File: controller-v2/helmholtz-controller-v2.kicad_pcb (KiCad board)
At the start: 2 copper layers, 72.7 x 72.1 mm, 60 parts, among them J1 Screw_Terminal_01x02, J2 Screw_Terminal_01x02, J3 Screw_Terminal_01x02, J4 Screw_Terminal_01x02, J5 Conn_01x04, U1 BDS63150AFM, U2 BDS63150AFM, U3 INA226, U4 INA226, U5 BDS63150AFM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

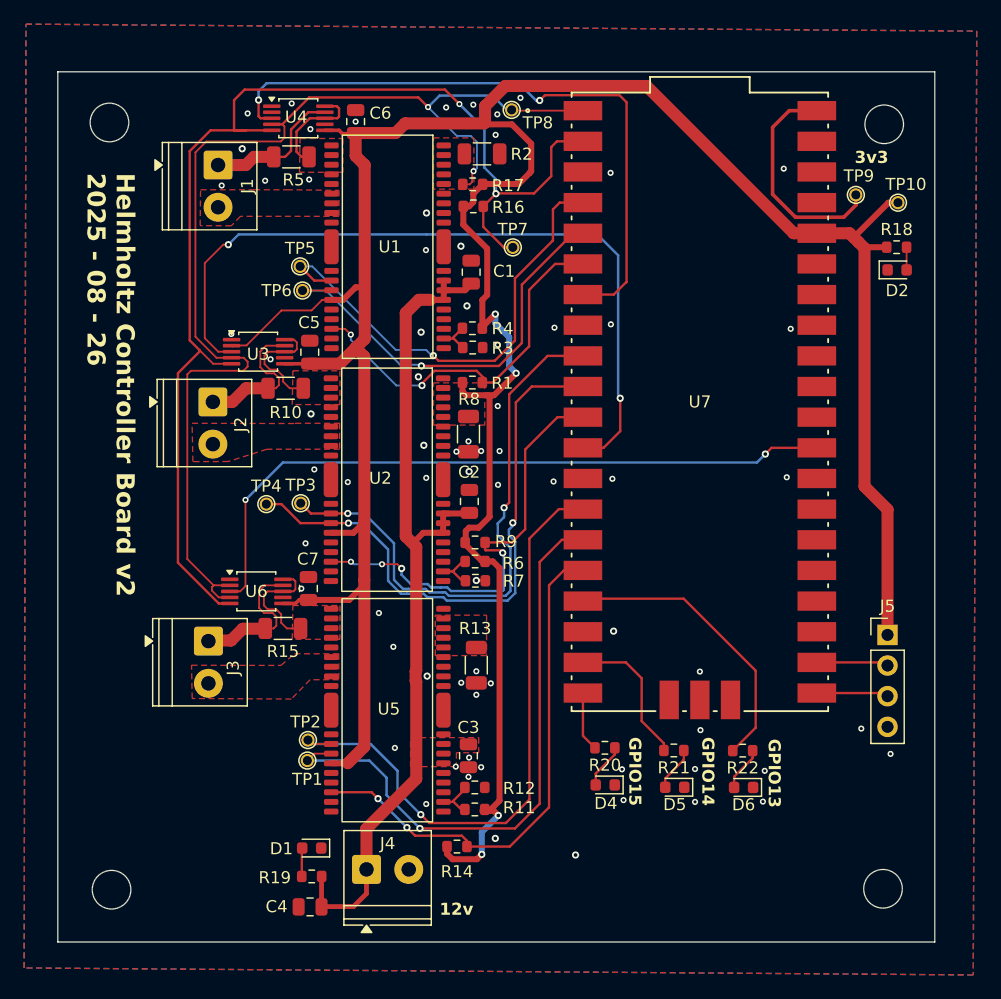
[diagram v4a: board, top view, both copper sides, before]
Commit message: Final cleanup of board before fab.
Did some polishing on layout for better power flow.
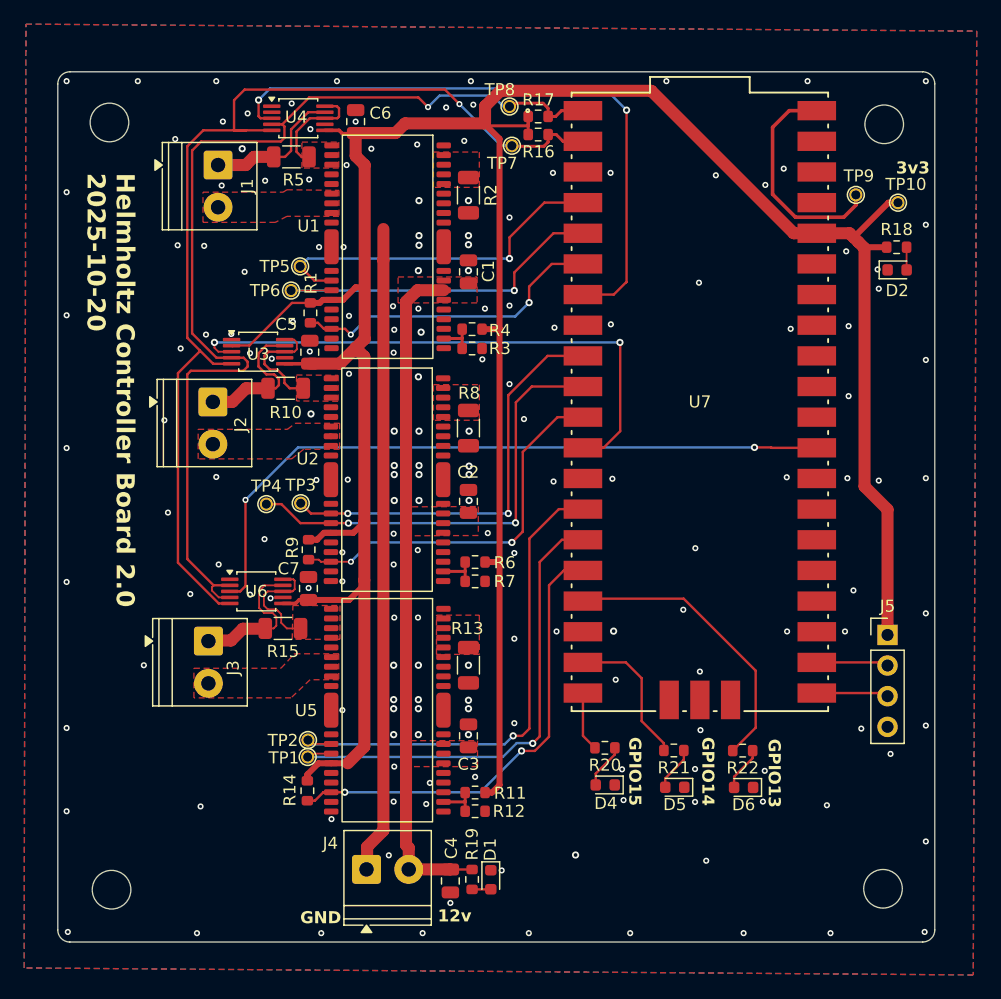
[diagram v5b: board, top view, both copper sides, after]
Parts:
- moved D1 15.1 mm to (224.6, 153.3), turned to -90 degrees
- moved R1 14.6 mm to (209.6, 106.3), turned to -90 degrees
- moved R9 13.8 mm to (209.4, 125.9), turned to 90 degrees
- moved R19 13.3 mm to (223.0, 153.2), turned to -90 degrees
- moved R14 13.2 mm to (209.3, 145.9), turned to 90 degrees
- moved C4 11.8 mm to (221.2, 153.4), turned to 90 degrees
- moved TP7 8.43 mm to (226.3, 92.5), turned to 180 degrees
- moved R16 8.02 mm to (228.5, 91.5)
- moved R17 7.81 mm to (228.5, 90.0), turned to 180 degrees
- moved R2 3.61 mm to (222.7, 96.5), turned to -90 degrees
- moved R12 1.98 mm to (223.2, 147.6)
- moved C3 1.65 mm to (222.7, 141.3), turned to -90 degrees
- moved R11 1.40 mm to (223.2, 146.1)
- moved TP6 0.95 mm to (208.0, 104.5)
- moved R13 0.65 mm to (222.7, 135.5)
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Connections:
- net Net-(U2-IN1) renamed /Y_IN1
- net Net-(U2-IN2) renamed /Y_IN2
- net Net-(U2-~{FAILA}) renamed /Y_FAIL
- net Net-(U3-~{Alert}) renamed /Y_INA_ALERT
- net Net-(U5-IN1) renamed /Z_IN1
- net Net-(U5-IN2) renamed /Z_IN2
- net Net-(U5-~{FAILA}) renamed /Z_FAIL
- net Net-(U6-~{Alert}) renamed /Z_INA_ALERT
- net Net-(U7-GPIO13) renamed /D6
- net Net-(U7-GPIO14) renamed /D5
- net Net-(U7-GPIO15) renamed /D4
- J4 pad 1: +12V -> GND
- J4 pad 2: GND -> +12V
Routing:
- net GND: track 2.82 -> 55.9 mm, vias 71 -> 178
- net /Y_INA_ALERT: track 63.2 -> 46.6 mm
- net +12V: track 71.3 -> 56.0 mm
- net +3.3V: track 263.5 -> 248.3 mm, vias 4 -> 0
- net SCL: track 100.1 -> 87.8 mm, vias 2 -> 1
- net /Y_IN1: track 47.1 -> 34.9 mm
- net /Y_IN2: track 48.1 -> 37.4 mm
- net /X_IN1: track 39.7 -> 29.7 mm
- net /Z_IN1: track 52.2 -> 42.4 mm
- net /Z_IN2: track 49.9 -> 40.9 mm
- net SDA: track 94.1 -> 86.0 mm, vias 2 -> 1
- net /Y_FAIL: track 37.2 -> 31.6 mm, vias 4 -> 2
- net /X_IN2: track 35.6 -> 30.4 mm
- net /Z_FAIL: track 43.3 -> 38.1 mm
- net /X_FAIL: track 30.9 -> 26.2 mm
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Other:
- outline, holes or cut-outs redrawn
- board text added: "GND"
- board text added: "Helmholtz Controller Board ${REVISION} ${ISSUE_DATE}"
- board text removed: "Helmholtz Controller Board v2 2025 - 08 - 26"

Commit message: Minor changes that bring the version to 2.1.
The 2.0 board is fabbed, and we found a few minor issues (wrong address listed in the schematic, no XYZ marking at pheonix connectors, etc).
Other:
- board text added: "X"
- board text added: "Y"
- board text added: "Z"
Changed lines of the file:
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@@
 	(title_block
 		(title "OreSat Helmholtz Cage Controller")
-		(date "2025-10-20")
-		(rev "2.0")
+		(date "2025-12-18")
+		(rev "2.1")
 		(company "Portland State Aerospace Society")
 	)
@@
 		)
 	)
+	(gr_text "Y"
+		(at 197.4 109.9 270)
+		(layer "F.SilkS")
+		(effects
+			(font
+				(size 1.5 1.5)
+				(thickness 0.3)
+				(bold yes)
+			)
+			(justify left bottom)
+		)
+	)
 	(gr_text "GPIO15\n"
 		(at 235.90625 141.44375 270)
@@
 		)
 	)
+	(gr_text "Z\n"
+		(at 197.1 129.75 270)
+		(layer "F.SilkS")
+		(effects
+			(font
+				(size 1.5 1.5)
+				(thickness 0.3)
+				(bold yes)
+			)
+			(justify left bottom)
+		)
+	)
 	(gr_text "GPIO13"
 		(at 247.45625 141.59375 270)
@@
 		)
 	)
+	(gr_text "X"
+		(at 197.3 99.65 270)
+		(layer "F.SilkS")
+		(effects
+			(font
+				(size 1.5 1.5)
+				(thickness 0.3)
+				(bold yes)
+			)
+			(justify left bottom)
+		)
+	)
+	(gr_text "Y"
+		(at 197.45 119.35 270)
+		(layer "F.SilkS")
+		(effects
+			(font
+				(size 1.5 1.5)
+				(thickness 0.3)
+				(bold yes)
+			)
+			(justify left bottom)
+		)
+	)
 	(gr_text "3v3"
 		(at 258.125 94.875 0)
@@
 				(bold yes)
 			)
+			(justify left bottom)
+		)
+	)
+	(gr_text "X"
+		(at 197.2 90.25 270)
+		(layer "F.SilkS")
+		(effects
+			(font
+				(size 1.5 1.5)
+				(thickness 0.3)
+				(bold yes)
+			)
+			(justify left bottom)
+		)
+	)
+	(gr_text "Z\n"
+		(at 197.1 139.15 270)
+		(layer "F.SilkS")
+		(effects
+			(font
+				(size 1.5 1.5)
+				(thickness 0.3)
+				(bold yes)
+			)
